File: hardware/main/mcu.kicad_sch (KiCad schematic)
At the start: 8 parts, among them U1 Holyiot-18010-NRF52840

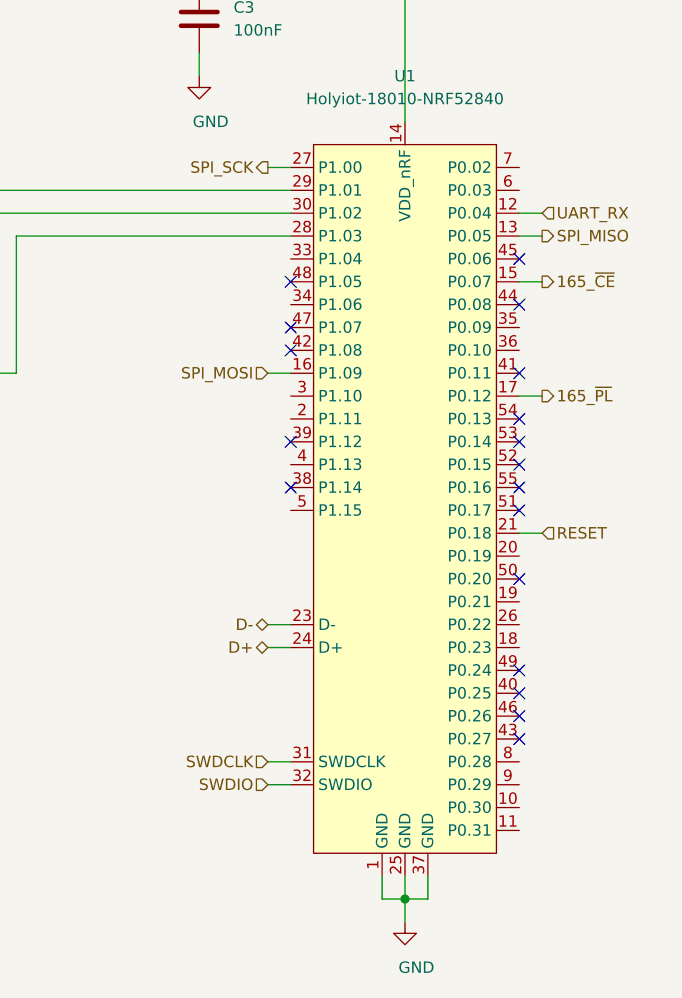
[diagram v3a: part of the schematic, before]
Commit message: Add no-connect-symbols to the NRF
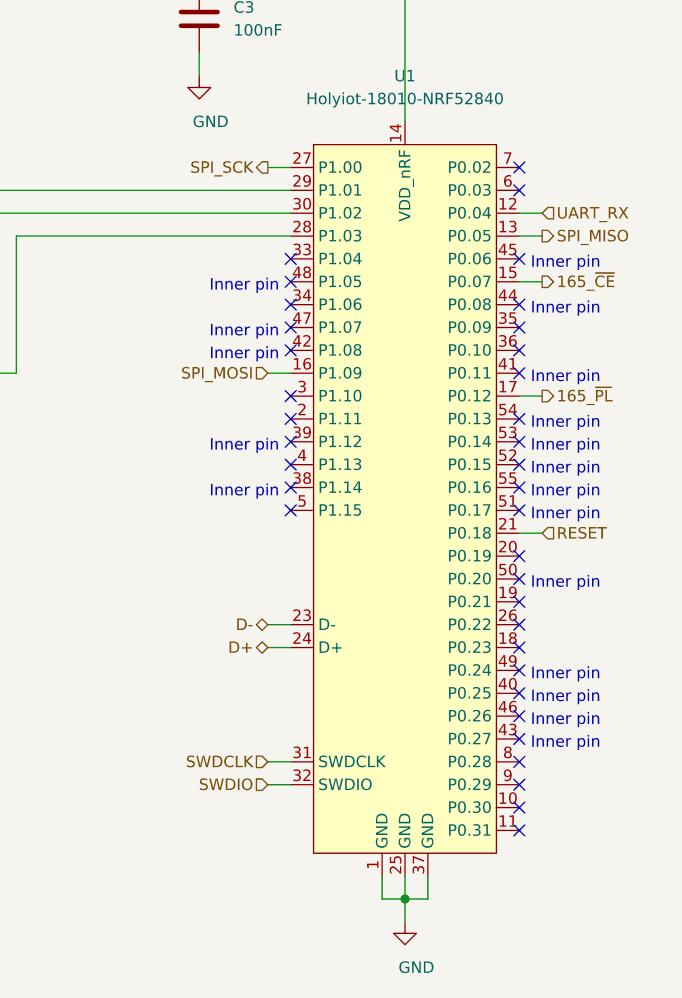
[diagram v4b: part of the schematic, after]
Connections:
- no-connect marks 18 -> 36
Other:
- note added: "Inner pin"
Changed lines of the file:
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@@
   (junction (at 139.7 29.21) (diameter 1.016) (color 0 0 0 0))
   (junction (at 139.7 130.81) (diameter 1.016) (color 0 0 0 0))
+  (no_connect (at 127 59.69))
+  (no_connect (at 127 64.77))
   (no_connect (at 152.4 64.77))
+  (no_connect (at 152.4 118.11))
   (no_connect (at 152.4 85.09))
   (no_connect (at 127 69.85))
+  (no_connect (at 152.4 120.65))
   (no_connect (at 127 62.23))
   (no_connect (at 152.4 59.69))
@@
   (no_connect (at 152.4 105.41))
   (no_connect (at 127 85.09))
+  (no_connect (at 152.4 115.57))
   (no_connect (at 152.4 72.39))
   (no_connect (at 152.4 113.03))
+  (no_connect (at 152.4 100.33))
+  (no_connect (at 152.4 49.53))
   (no_connect (at 152.4 95.25))
   (no_connect (at 127 80.01))
   (no_connect (at 152.4 80.01))
+  (no_connect (at 152.4 52.07))
   (no_connect (at 152.4 87.63))
   (no_connect (at 127 67.31))
+  (no_connect (at 152.4 67.31))
+  (no_connect (at 127 87.63))
+  (no_connect (at 152.4 92.71))
+  (no_connect (at 127 74.93))
+  (no_connect (at 152.4 69.85))
+  (no_connect (at 127 77.47))
+  (no_connect (at 152.4 97.79))
+  (no_connect (at 152.4 123.19))
+  (no_connect (at 152.4 102.87))
   (no_connect (at 152.4 77.47))
+  (no_connect (at 127 82.55))
   (no_connect (at 152.4 110.49))
   (no_connect (at 152.4 82.55))
@@
     (stroke (width 0) (type solid) (color 0 0 0 0))
   )
+  (text "Inner pin" (at 125.73 63.5 180)
+    (effects (font (size 1.27 1.27)) (justify right bottom))
+  )
+  (text "Inner pin" (at 125.73 68.58 180)
+    (effects (font (size 1.27 1.27)) (justify right bottom))
+  )
+  (text "Inner pin" (at 125.73 71.12 180)
+    (effects (font (size 1.27 1.27)) (justify right bottom))
+  )
+  (text "Inner pin" (at 125.73 81.28 180)
+    (effects (font (size 1.27 1.27)) (justify right bottom))
+  )
+  (text "Inner pin" (at 125.73 86.36 180)
+    (effects (font (size 1.27 1.27)) (justify right bottom))
+  )
+  (text "Inner pin" (at 153.67 60.96 0)
+    (effects (font (size 1.27 1.27)) (justify left bottom))
+  )
+  (text "Inner pin" (at 153.67 66.04 0)
+    (effects (font (size 1.27 1.27)) (justify left bottom))
+  )
+  (text "Inner pin" (at 153.67 73.66 0)
+    (effects (font (size 1.27 1.27)) (justify left bottom))
+  )
+  (text "Inner pin" (at 153.67 78.74 0)
+    (effects (font (size 1.27 1.27)) (justify left bottom))
+  )
+  (text "Inner pin" (at 153.67 81.28 0)
+    (effects (font (size 1.27 1.27)) (justify left bottom))
+  )
+  (text "Inner pin" (at 153.67 83.82 0)
+    (effects (font (size 1.27 1.27)) (justify left bottom))
+  )
+  (text "Inner pin" (at 153.67 86.36 0)
+    (effects (font (size 1.27 1.27)) (justify left bottom))
+  )
+  (text "Inner pin" (at 153.67 88.9 0)
+    (effects (font (size 1.27 1.27)) (justify left bottom))
+  )
+  (text "Inner pin" (at 153.67 96.52 0)
+    (effects (font (size 1.27 1.27)) (justify left bottom))
+  )
+  (text "Inner pin" (at 153.67 106.68 0)
+    (effects (font (size 1.27 1.27)) (justify left bottom))
+  )
+  (text "Inner pin" (at 153.67 109.22 0)
+    (effects (font (size 1.27 1.27)) (justify left bottom))
+  )
+  (text "Inner pin" (at 153.67 111.76 0)
+    (effects (font (size 1.27 1.27)) (justify left bottom))
+  )
+  (text "Inner pin" (at 153.67 114.3 0)
+    (effects (font (size 1.27 1.27)) (justify left bottom))
+  )
   (hierarchical_label "SPI_SCK" (shape output) (at 124.46 49.53 180)

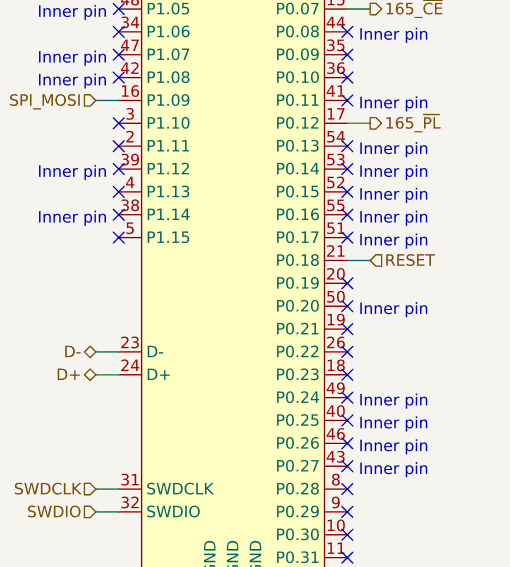
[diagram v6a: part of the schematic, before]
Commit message: Add a line for the UART direction main->numpad
This is necessary as the numlock-led is situated on the numpad and the
main mcu has to be able to switch it on and off.
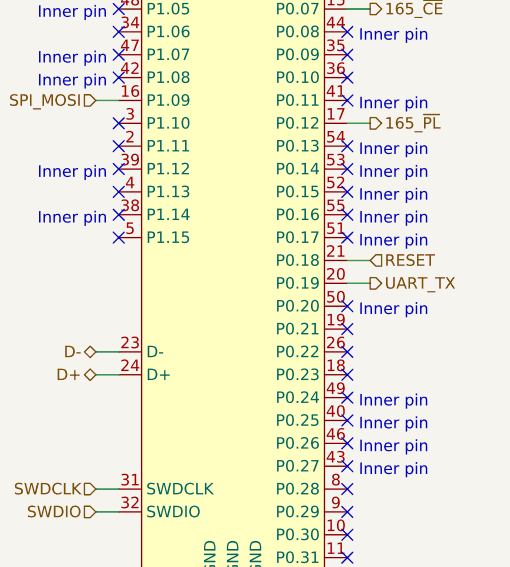
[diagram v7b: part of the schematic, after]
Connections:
- net UART_TX: now reaches U1.20 (P0.19)
- no-connect marks 36 -> 35
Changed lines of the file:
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@@
   (junction (at 139.7 29.21) (diameter 1.016) (color 0 0 0 0))
   (junction (at 139.7 130.81) (diameter 1.016) (color 0 0 0 0))
+  (no_connect (at 152.4 113.03))
+  (no_connect (at 152.4 123.19))
+  (no_connect (at 127 67.31))
+  (no_connect (at 152.4 120.65))
+  (no_connect (at 152.4 97.79))
+  (no_connect (at 152.4 102.87))
+  (no_connect (at 152.4 95.25))
+  (no_connect (at 152.4 67.31))
+  (no_connect (at 127 74.93))
+  (no_connect (at 152.4 100.33))
+  (no_connect (at 152.4 105.41))
+  (no_connect (at 152.4 107.95))
+  (no_connect (at 152.4 82.55))
+  (no_connect (at 152.4 52.07))
+  (no_connect (at 127 59.69))
+  (no_connect (at 127 69.85))
+  (no_connect (at 127 77.47))
+  (no_connect (at 152.4 49.53))
+  (no_connect (at 152.4 115.57))
+  (no_connect (at 127 80.01))
+  (no_connect (at 152.4 69.85))
+  (no_connect (at 152.4 59.69))
+  (no_connect (at 152.4 118.11))
+  (no_connect (at 152.4 110.49))
+  (no_connect (at 127 62.23))
+  (no_connect (at 127 87.63))
+  (no_connect (at 152.4 85.09))
   (no_connect (at 152.4 77.47))
-  (no_connect (at 127 87.63))
-  (no_connect (at 152.4 59.69))
-  (no_connect (at 152.4 107.95))
-  (no_connect (at 152.4 110.49))
-  (no_connect (at 152.4 67.31))
-  (no_connect (at 152.4 95.25))
+  (no_connect (at 152.4 87.63))
+  (no_connect (at 127 64.77))
+  (no_connect (at 152.4 64.77))
   (no_connect (at 152.4 80.01))
-  (no_connect (at 152.4 102.87))
-  (no_connect (at 127 67.31))
-  (no_connect (at 127 80.01))
-  (no_connect (at 127 77.47))
-  (no_connect (at 152.4 123.19))
-  (no_connect (at 152.4 69.85))
-  (no_connect (at 127 59.69))
-  (no_connect (at 152.4 105.41))
-  (no_connect (at 152.4 49.53))
-  (no_connect (at 152.4 85.09))
-  (no_connect (at 152.4 118.11))
-  (no_connect (at 152.4 97.79))
-  (no_connect (at 127 69.85))
-  (no_connect (at 152.4 64.77))
-  (no_connect (at 127 64.77))
-  (no_connect (at 152.4 52.07))
-  (no_connect (at 152.4 92.71))
-  (no_connect (at 152.4 87.63))
+  (no_connect (at 127 85.09))
   (no_connect (at 152.4 72.39))
-  (no_connect (at 127 85.09))
-  (no_connect (at 152.4 100.33))
-  (no_connect (at 152.4 120.65))
   (no_connect (at 127 82.55))
-  (no_connect (at 152.4 113.03))
-  (no_connect (at 152.4 115.57))
-  (no_connect (at 127 62.23))
-  (no_connect (at 127 74.93))
-  (no_connect (at 152.4 82.55))
   (wire (pts (xy 71.12 52.07) (xy 73.66 52.07))
     (stroke (width 0) (type solid) (color 0 0 0 0))
@@
     (stroke (width 0) (type solid) (color 0 0 0 0))
   )
+  (wire (pts (xy 152.4 92.71) (xy 154.94 92.71))
+    (stroke (width 0) (type solid) (color 0 0 0 0))
+  )
   (wire (pts (xy 154.94 57.15) (xy 152.4 57.15))
     (stroke (width 0) (type solid) (color 0 0 0 0))
@@
     (effects (font (size 1.27 1.27)) (justify left))
   )
+  (hierarchical_label "UART_TX" (shape output) (at 154.94 92.71 0)
+    (effects (font (size 1.27 1.27)) (justify left))
+  )
